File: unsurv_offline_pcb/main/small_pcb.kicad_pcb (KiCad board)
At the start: 4 copper layers, 35 x 45 mm, 60 parts, among them J1 USB_B_Micro, J2 S2B-PH-SM4-TB_LF__SN_, J3 1.27mm_female_connector, Q1 Q_PMOS_GSD, Q2 UMH3N, SW1 SW_DIP_x01, U1 MCP73831-2-OT, U3 AP2112K-3.3, U4 MPU-6050_NRND, U5 ESP32-WROOM-32, U6 CAM-M8C-0-10, U7 CH340G, U8 RF430CL330H

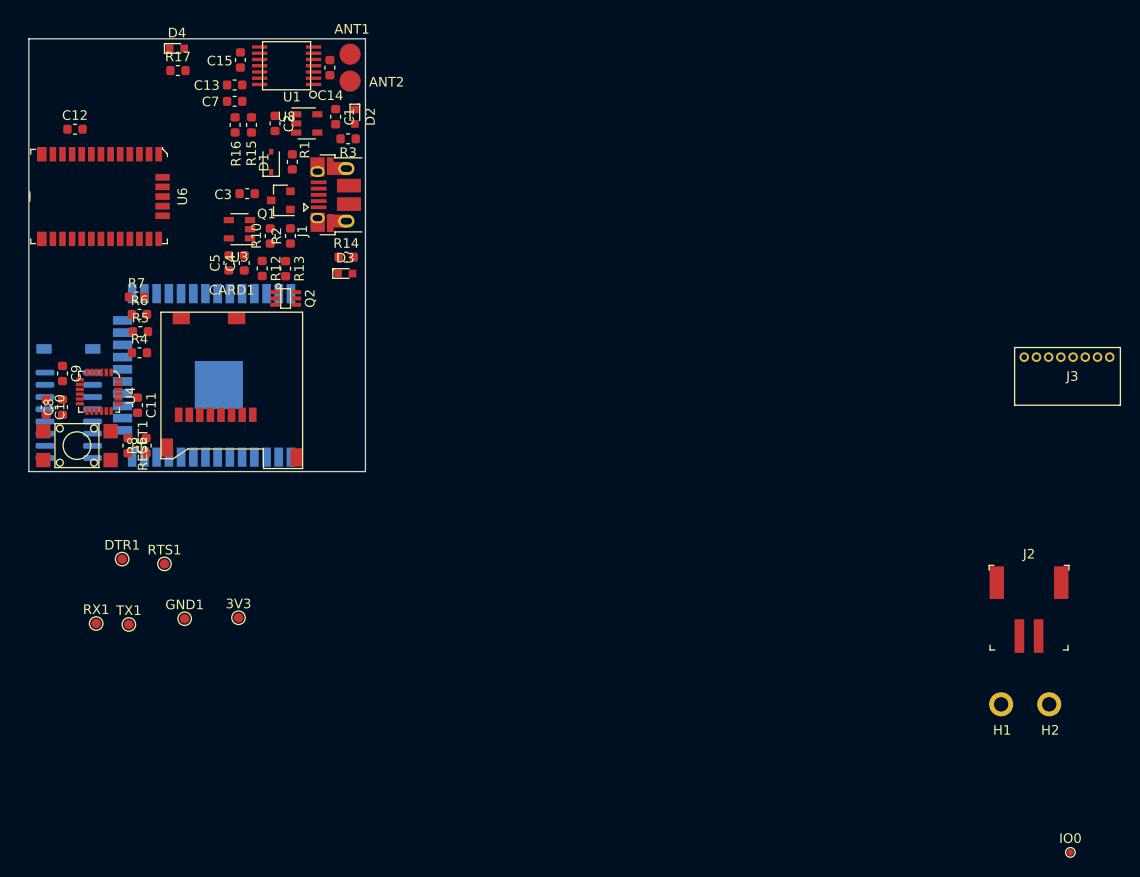
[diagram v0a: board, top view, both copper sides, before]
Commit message: reduced pcb size
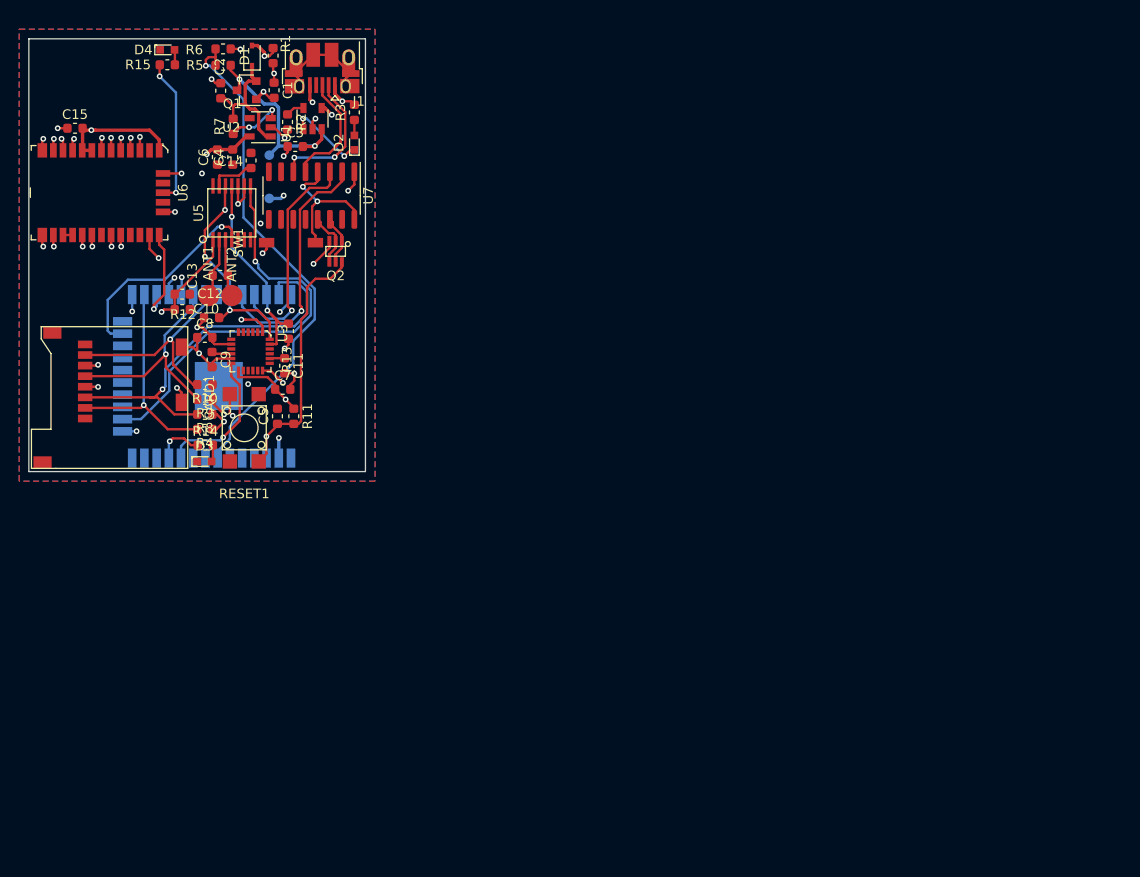
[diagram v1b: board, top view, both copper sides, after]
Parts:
- removed 3V3, DTR1, GND1, RTS1, RX1, TX1: TestPoint, TestPoint:TestPoint_Pad_D1.0mm
- removed the C10 at (51.8, 88.3)
- removed the C6 at (60.3, 92.3)
- removed H1, H2: MountingHole_Pad, unsurv_offline_pcb_footprints:MountingHole_1.5mm_hole_in_FPaste
- removed IO0: TestPoint, unsurv_offline_pcb_footprints:TestPoint_Pad_D0.7mm
- removed J2: S2B-PH-SM4-TB_LF__SN_, digikey-footprints:PinHeader_2x1mm_P2mm_SMD_RA
- removed J3: 1.27mm_female_connector, unsurv_offline_pcb_footprints:LPPB081NGCN-RC
- removed the R8 at (62.2, 92.3)
- removed the U5 at (69.0, 85.0)
- added BATT+1: +, TestPoint:TestPoint_Pad_D1.0mm, B.Cu at (75.0, 62.1)
- added BATT-1: -, TestPoint:TestPoint_Pad_D1.0mm, B.Cu at (75.0, 66.6)
- added C5: 100nF, Capacitor_SMD:C_0603_1608Metric, F.Cu at (75.8, 89.2)
- added C7: 0.1yF, Capacitor_SMD:C_0603_1608Metric, F.Cu at (76.4, 86.5)
- added R11: 10k, Resistor_SMD:R_0603_1608Metric, F.Cu at (77.5, 89.2)
- added U3: MPU-6050_NRND, digikey-footprints:QFN-24-1EP_4x4mm, F.Cu at (73.0, 82.5)
- C8: value 0.1yF -> 10nF
- C9: value 10nF -> 0.1yF
- SW1, U7: moved to F.Cu
- U4: value MPU-6050_NRND -> ESP32-WROOM-32; footprint digikey-footprints:QFN-24-1EP_4x4mm -> RF_Module:ESP32-WROOM-32; moved to B.Cu
- moved U7 34.1 mm to (79.4, 66.3), turned to 270 degrees
- moved ANT2 28.0 mm to (71.1, 76.7), turned to 90 degrees
- moved ANT1 26.7 mm to (68.7, 76.7), turned to 90 degrees
- moved SW1 25.7 mm to (79.8, 71.2), turned to 90 degrees
- moved D3 24.4 mm to (68.3, 94.0)
- moved R14 24.4 mm to (68.3, 92.2)
- moved C13 24.4 mm to (69.9, 74.6), turned to 0 degrees
- moved C12 22.4 mm to (66.0, 76.5), turned to 0 degrees
- moved C10 22.3 mm to (66.0, 78.2), turned to 0 degrees
- moved RESET1 17.5 mm to (72.4, 90.5), turned to 180 degrees
- moved C8 16.5 mm to (68.3, 81.0), turned to 0 degrees
- moved U5 16.3 mm to (71.1, 68.1), turned to 90 degrees
- moved C11 15.8 mm to (76.6, 84.0)
- moved C9 15.6 mm to (69.0, 83.3)
- moved J1 13.2 mm to (80.5, 53.0), turned to 180 degrees
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- renumbered C7 to C10, C13 to C12, C14 to C13, C15 to C14, C12 to C15, C3 to C2, C2 to C3, C5 to C6, R7 to R10, R17 to R15, R15 to R5, R16 to R6, R10 to R7, R5 to R8, R6 to R9, U3 to U2, U8 to U5
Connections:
- C8 pad 1: +3V3 -> GND
- C8 pad 2: GND -> +3V3
- C9 pad 1: GND -> Net-(C9-Pad1)
- C9 pad 2: +3V3 -> GND
- U4 pad 10: Net-(C10-Pad1) -> ACC_INT
- U4 pad 11: GND -> 26
- U4 pad 12: ACC_INT -> 27
- U4 pad 13: +3V3 -> 14
- U4 pad 14: Net-(U4-Pad14) -> 12
- U4 pad 15: Net-(U4-Pad15) -> GND
- U4 pad 16: Net-(U4-Pad16) -> 13
- U4 pad 18: GND -> Net-(U4-Pad18)
- U4 pad 2: Net-(U4-Pad2) -> +3V3
- U4 pad 20: Net-(C11-Pad1) -> Net-(U4-Pad20)
- U4 pad 23: SCL -> 15
- U4 pad 24: SDA -> Net-(U4-Pad24)
- U4 pad 3: Net-(U4-Pad3) -> RESET
- U4 pad 7: Net-(U4-Pad7) -> 35
- U4 pad 8: +3V3 -> Net-(U4-Pad8)
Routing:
- net GND: track 0.00 -> 64.7 mm, vias 0 -> 37
- net +3V3: track 0.00 -> 55.2 mm, vias 0 -> 11
- net 35: track 0.00 -> 53.4 mm, vias 0 -> 1
- net SCL: track 0.00 -> 45.6 mm, vias 0 -> 3
- net 13: track 0.00 -> 43.1 mm, vias 0 -> 1
- net SDA: track 0.00 -> 41.8 mm, vias 0 -> 4
- net 23: track 0.00 -> 40.3 mm, vias 0 -> 1
- net 5: track 0.00 -> 37.6 mm, vias 0 -> 2
- net 0: track 0.00 -> 29.6 mm, vias 0 -> 2
- net RESET: track 0.00 -> 28.8 mm, vias 0 -> 1
- net RX0: track 0.00 -> 25.8 mm, vias 0 -> 1
- net 4: track 0.00 -> 24.3 mm, vias 0 -> 1
- net TX0: track 0.00 -> 23.5 mm, vias 0 -> 1
- net 18: track 0.00 -> 22.9 mm, vias 0 -> 1
- net 15: track 0.00 -> 22.1 mm, vias 0 -> 1
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- added copper zone on PWR, net +3V3
- added copper zone on PWR, net +5V
- added copper zone on B.Cu, net GND
- added copper zone on F.Cu, net GND
- added copper zone on GND, net GND

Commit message: finalized smaller pcb
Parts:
- renumbered BATT+1 to +, BATT-1 to -, RESET1 to RST
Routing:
- net GND: track 64.7 -> 67.9 mm, vias 37 -> 39
- net RESET: track 28.8 -> 29.4 mm

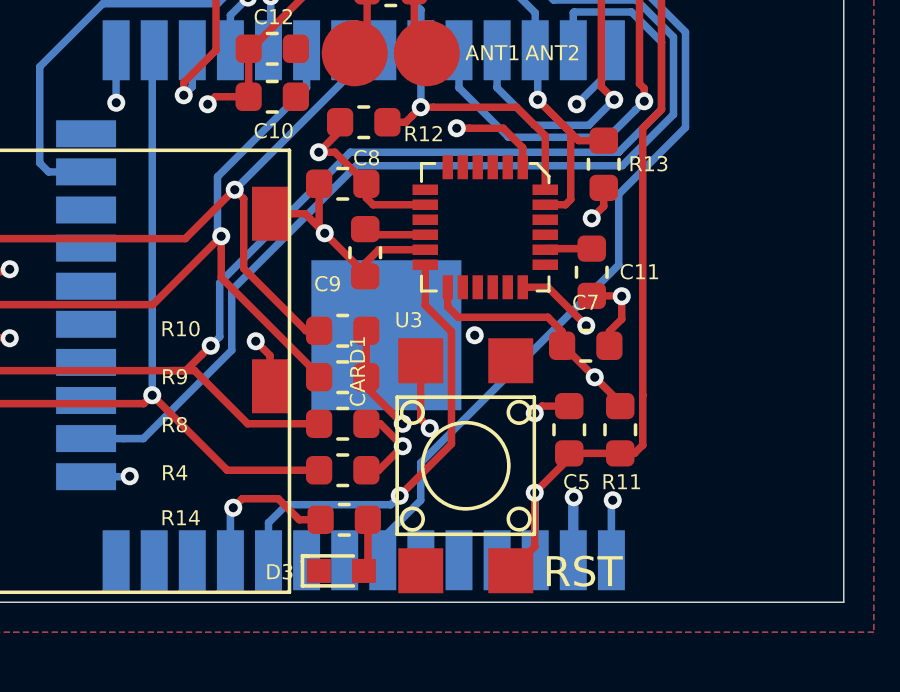
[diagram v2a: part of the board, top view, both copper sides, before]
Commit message: added motion activation + code refactoring
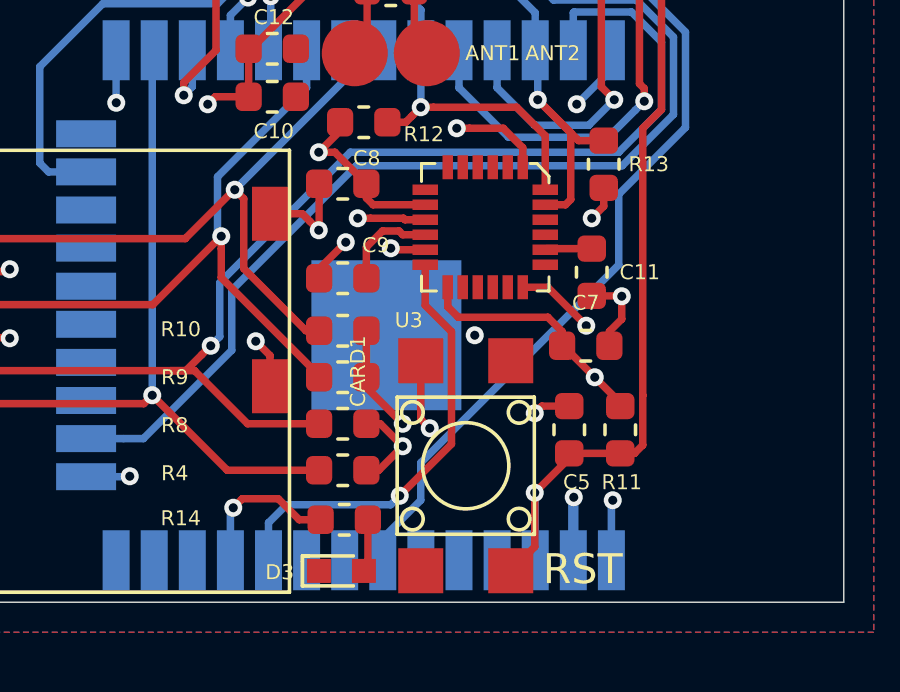
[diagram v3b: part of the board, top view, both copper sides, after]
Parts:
- R2: value 2k -> 10k
- moved C9 1.13 mm to (68.3, 84.2), turned to 180 degrees
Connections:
- U3 pad 9: Net-(U3-Pad9) -> GND
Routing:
- net Net-(C9-Pad1): track 2.08 -> 3.36 mm
- net GND: vias 39 -> 42
